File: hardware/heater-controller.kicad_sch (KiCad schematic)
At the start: 9 parts, among them J1 Vitotronic plug 96, Q1 SFH 309 FA

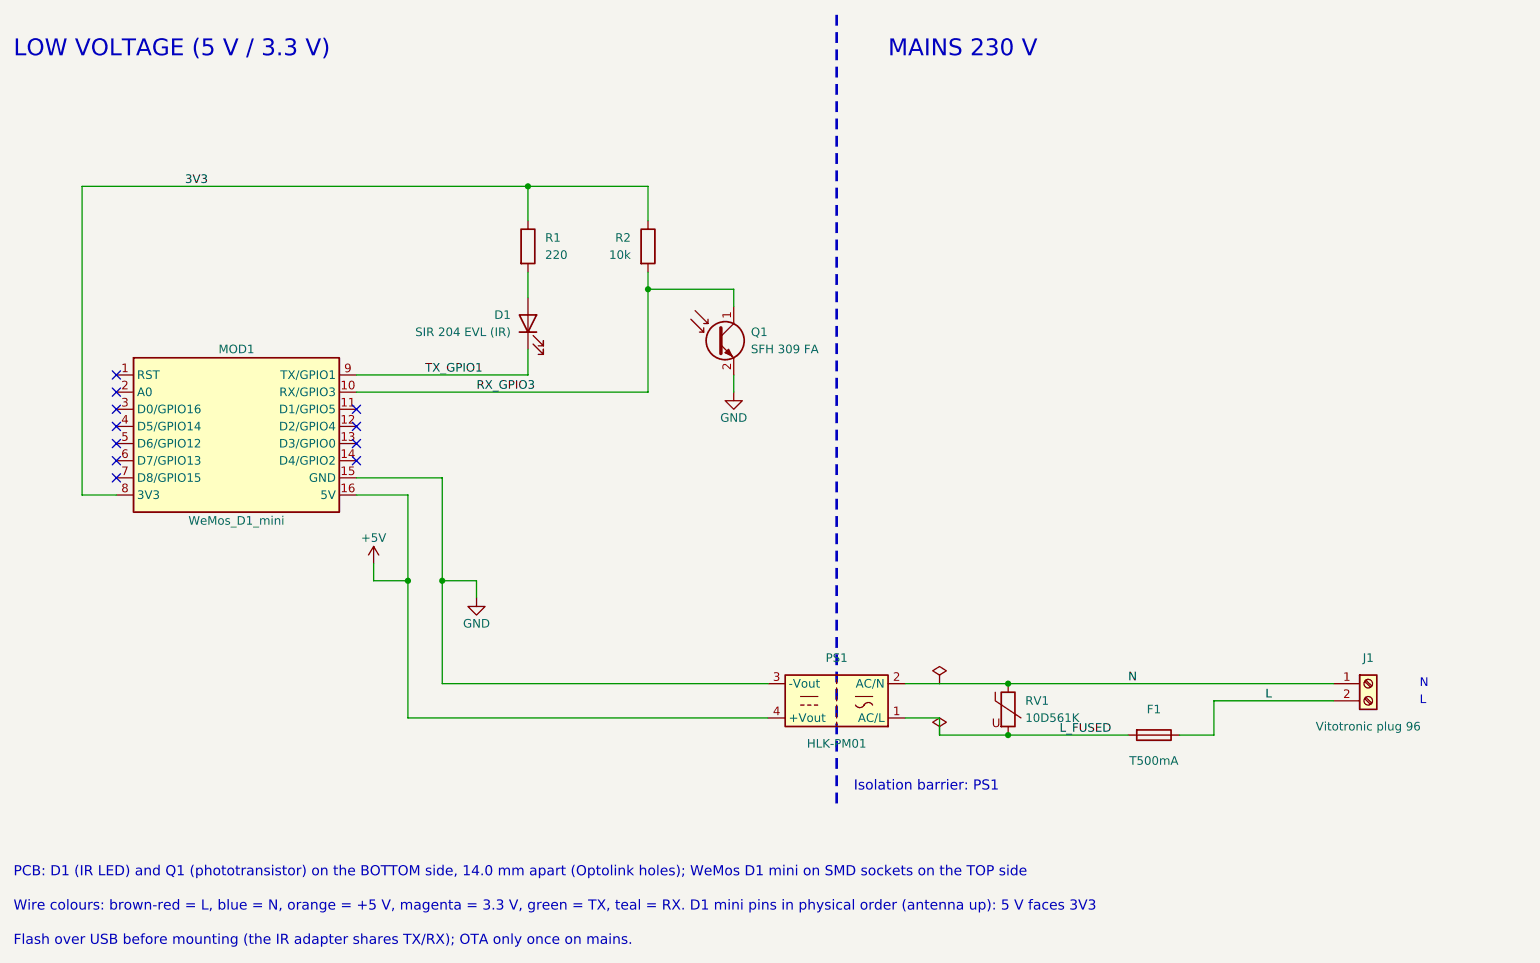
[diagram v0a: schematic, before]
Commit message: feat(hardware): move to ESP32-C3 on a removable U-shaped board
- ESP32-C3 super mini replaces the D1 mini: Optolink UART on GPIO4/GPIO3,
  logs over native USB
- inverted U board (86 x 39.5 mm): 230 V leg, optical head header on the bar,
  C3 on SMD female sockets; screw terminal for the mains wires
- off-board optical head on a 4-wire ribbon
- back GND pour, 0.7 mm power tracks, 6 mm mains isolation checked by DRC
- C3 socket footprint generator and fabrication export script
- enclosure redrawn around the new board
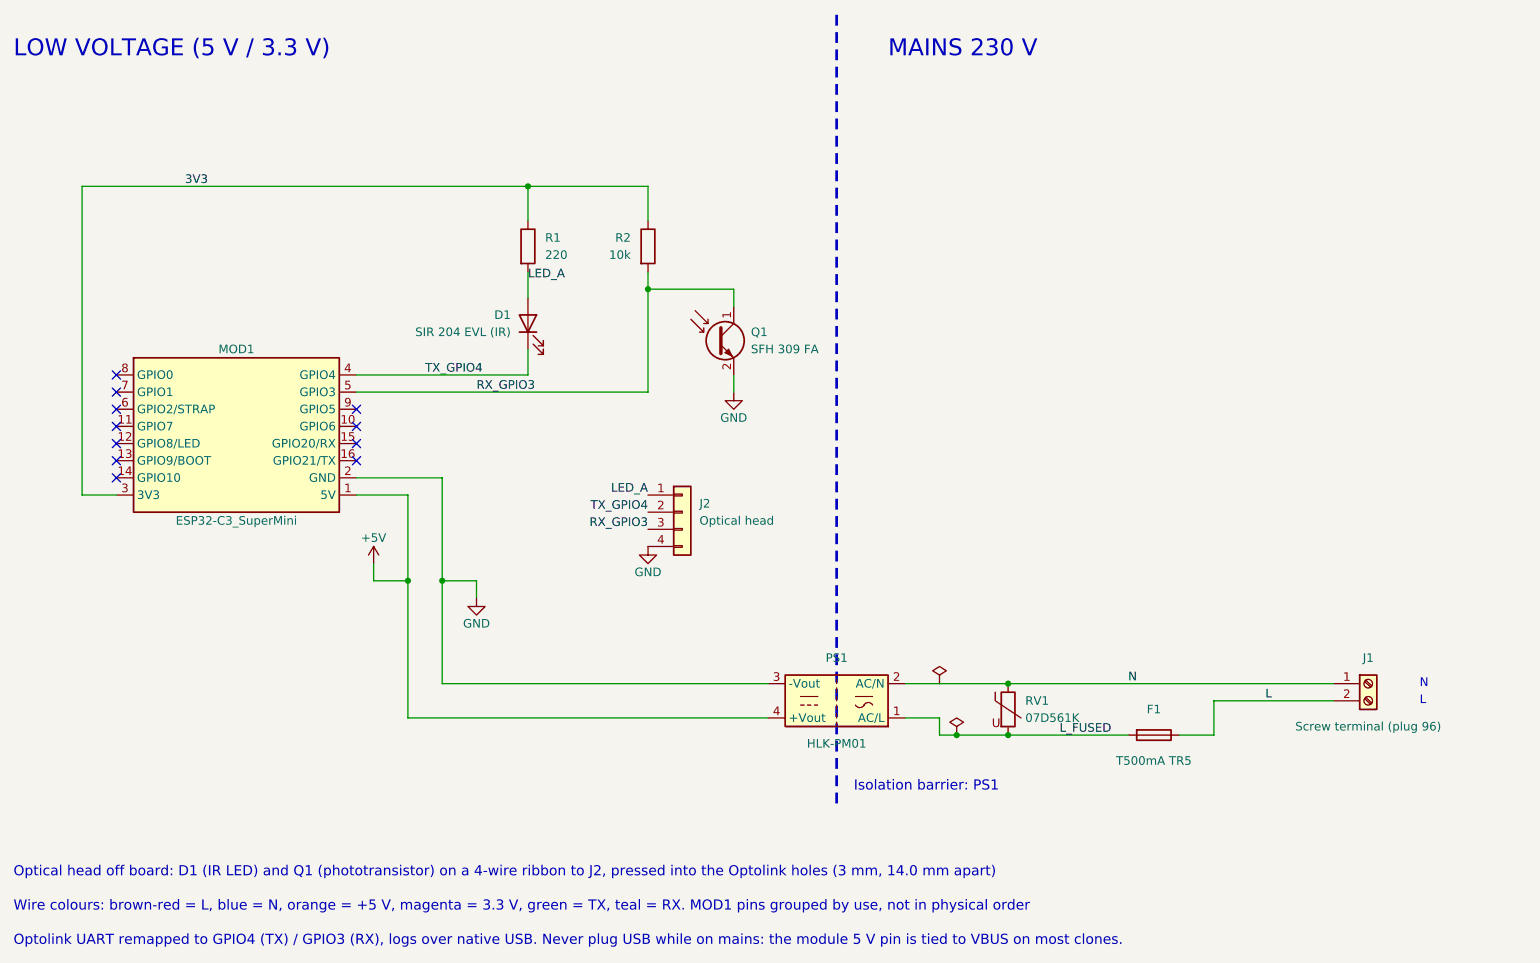
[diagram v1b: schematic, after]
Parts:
- added J2: Optical head, Connector_PinHeader_2.54mm:PinHeader_1x04_P2.54mm_Vertical, symbol Connector_Generic:Conn_01x04
- F1: value T500mA -> T500mA TR5; footprint Fuse:Fuseholder_Cylinder-5x20mm_Bulgin_FX0456_Vertical_Closed -> Fuse:Fuseholder_TR5_Littelfuse_No560_No460
- J1: value Vitotronic plug 96 -> Screw terminal (plug 96)
- MOD1: value WeMos_D1_mini -> ESP32-C3_SuperMini; footprint heater-controller:WEMOS_D1_mini_SMD_sockets -> heater-controller:ESP32-C3_SuperMini_Sockets; symbol heater-controller:WeMos_D1_mini -> heater-controller:ESP32-C3_SuperMini
- RV1: value 10D561K -> 07D561K; footprint Varistor:RV_Disc_D12mm_W4.2mm_P7.5mm -> Varistor:RV_Disc_D9mm_W4.1mm_P5mm
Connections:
- net +5V: now also MOD1.1 (5V); no longer MOD1.16 (5V)
- net 3V3: now also MOD1.3 (3V3); no longer MOD1.8 (3V3)
- net GND: now also MOD1.2 (GND), J2.4 (Pin_4); no longer MOD1.15 (GND)
- net RX_GPIO3: now also MOD1.5 (GPIO3), J2.3 (Pin_3); no longer MOD1.10 (RX/GPIO3)
- net TX_GPIO4: now reaches MOD1.4 (GPIO4)
- net TX_GPIO4: now also D1.1 (K), J2.2 (Pin_2)
- net LED_A: now reaches D1.2 (A), R1.2
- net LED_A: now also J2.1 (Pin_1)
- net TX_GPIO1: no longer names the net of MOD1.9 (GPIO5)
- net TX_GPIO1: no longer D1.1 (K)
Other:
- note added: "Optical head off board: D1 (IR LED) and Q1 (phototransistor) on a 4-wire ribbon to J2, pressed into the Optolink holes (3 mm, 14.0 mm apart)"
- note added: "Optolink UART remapped to GPIO4 (TX) / GPIO3 (RX), logs over native USB. Never plug USB while on mains: the module 5 V pin is tied to VBUS on most clones."
- note added: "Wire colours: brown-red = L, blue = N, orange = +5 V, magenta = 3.3 V, green = TX, teal = RX. MOD1 pins grouped by use, not in physical order"
- note removed: "Flash over USB before mounting (the IR adapter shares TX/RX); OTA only once on mains."
- note removed: "PCB: D1 (IR LED) and Q1 (phototransistor) on the BOTTOM side, 14.0 mm apart (Optolink holes); WeMos D1 mini on SMD sockets on the TOP side"
- note removed: "Wire colours: brown-red = L, blue = N, orange = +5 V, magenta = 3.3 V, green = TX, teal = RX. D1 mini pins in physical order (antenna up): 5 V faces 3V3"

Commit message: feat(hardware): hand-solderable board with SMD C3 sockets for JLCPCB
- C3 plugged into two hanxia 1x8 SMD sockets (J3/J4) at 15.24 mm, the only
  parts with an LCSC number; MOD1 off board with a board-only outline
- through-hole everything else: TR5 T1A fuse, 07D431K varistor, JST PH
  vertical optical head connector, axial resistors
- HLK-PM01 footprint from the Hi-Link datasheet (15.4 / 29.4 mm pin pitch)
- footprints generated by footprints.py from the datasheets
- export adds the JLCPCB BOM and placement files
- routing done in KiCad: 0.7 mm power tracks, no ground plane
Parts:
- added J3: Socket 1x8 SMD (C3 pins 1-8), heater-controller:PinSocket_1x08_P2.54mm_SMD_HX-ZQ, symbol Connector_Generic:Conn_01x08
- added J4: Socket 1x8 SMD (C3 pins 9-16), heater-controller:PinSocket_1x08_P2.54mm_SMD_HX-ZQ, symbol Connector_Generic:Conn_01x08
- D1, Q1: now left out of the parts list
- F1: value T500mA TR5 -> T1A TR5
- J2: value Optical head -> Optical head JST PH 4P; footprint Connector_PinHeader_2.54mm:PinHeader_1x04_P2.54mm_Vertical -> Connector_JST:JST_PH_B4B-PH-K_1x04_P2.00mm_Vertical
- MOD1: footprint heater-controller:ESP32-C3_SuperMini_Sockets -> (none); now left out of the parts list
- PS1: footprint Converter_ACDC:Converter_ACDC_Hi-Link_HLK-PMxx -> heater-controller:Converter_ACDC_HLK-PM01
- R1, R2: footprint Resistor_SMD:R_0805_2012Metric -> Resistor_THT:R_Axial_DIN0207_L6.3mm_D2.5mm_P7.62mm_Horizontal
- RV1: value 07D561K -> 07D431K (275VAC); footprint Varistor:RV_Disc_D9mm_W4.1mm_P5mm -> Varistor:RV_Disc_D7mm_W4.3mm_P5mm
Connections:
- net +5V: now also J3.1 (Pin_1)
- net 3V3: now also J3.3 (Pin_3)
- net GND: now also J3.2 (Pin_2)
- net RX_GPIO3: now also J3.5 (Pin_5)
- net TX_GPIO4: now also J3.4 (Pin_4)
- no-connect marks 11 -> 22

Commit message: feat(hardware): source every part at LCSC with datasheet footprints
- Kefa KF128 terminal block (Phoenix MKDS out of stock), Bourns MOV-07D431K
  inline varistor and JST PH with 0.9 mm holes, drawn by footprints.py
- LCSC number on every part; split-bom.py writes the JLCPCB BOM (SMD only)
  and an LCSC cart for the hand-soldered parts
- RV1 rerouted for its inline leads; DRC clean, schematic parity
- Enclosure split into named bodies: shells, lid, optical plug
- READMEs: parts list with suppliers, prices and footprint specs
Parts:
- F1: value T1A TR5 -> TR5 holder + T1A fuse; LCSC (none) -> C142909
- J1: value Screw terminal (plug 96) -> KF128-5.08 (plug 96); footprint TerminalBlock_Phoenix:TerminalBlock_Phoenix_MKDS-1,5-2-5.08_1x02_P5.08mm_Horizontal -> heater-controller:TerminalBlock_Kefa_KF128-5.08_1x02; LCSC (none) -> C474952
- J2: value Optical head JST PH 4P -> JST B4B-PH-K (optical head); footprint Connector_JST:JST_PH_B4B-PH-K_1x04_P2.00mm_Vertical -> heater-controller:JST_PH_B4B-PH-K_1x04_P2.00mm_Vertical_Drill0.9; LCSC (none) -> C131334
- PS1: LCSC (none) -> C209903
- RV1: value 07D431K (275VAC) -> MOV-07D431K (275VAC); footprint Varistor:RV_Disc_D7mm_W4.3mm_P5mm -> heater-controller:RV_Disc_D9mm_W4.8mm_P5mm_Inline; LCSC (none) -> C1528105
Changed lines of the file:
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@@
 			)
 		)
-		(property "Value" "Screw terminal (plug 96)"
+		(property "Value" "KF128-5.08 (plug 96)"
 			(at 231.14 130.81 0)
 			(show_name no)
@@
 			)
 		)
-		(property "Footprint" "TerminalBlock_Phoenix:TerminalBlock_Phoenix_MKDS-1,5-2-5.08_1x02_P5.08mm_Horizontal"
+		(property "Footprint" "heater-controller:TerminalBlock_Kefa_KF128-5.08_1x02"
 			(at 231.14 124.46 0)
 			(hide yes)
@@
 			)
 		)
+		(property "LCSC" "C474952"
+			(at 231.14 124.46 0)
+			(effects
+				(font
+					(size 1.27 1.27)
+				)
+				(hide yes)
+			)
+		)
 		(property "Description" ""
 			(at 231.14 124.46 0)
@@
 			)
 		)
-		(property "Value" "07D431K (275VAC)"
+		(property "Value" "MOV-07D431K (275VAC)"
 			(at 180.34 129.54 0)
 			(show_name no)
@@
 			)
 		)
-		(property "Footprint" "Varistor:RV_Disc_D7mm_W4.3mm_P5mm"
+		(property "Footprint" "heater-controller:RV_Disc_D9mm_W4.8mm_P5mm_Inline"
 			(at 177.8 128.27 0)
 			(hide yes)
@@
 			)
 		)
+		(property "LCSC" "C1528105"
+			(at 177.8 128.27 0)
+			(effects
+				(font
+					(size 1.27 1.27)
+				)
+				(hide yes)
+			)
+		)
 		(property "Description" ""
 			(at 177.8 128.27 0)
@@
 			)
 		)
+		(property "LCSC" "C209903"
+			(at 152.4 127 0)
+			(effects
+				(font
+					(size 1.27 1.27)
+				)
+				(hide yes)
+			)
+		)
 		(property "Description" ""
 			(at 152.4 127 0)
@@
 			)
 		)
-		(property "Value" "T1A TR5"
+		(property "Value" "TR5 holder + T1A fuse"
 			(at 199.39 135.89 90)
 			(show_name no)
@@
 			)
 		)
+		(property "LCSC" "C142909"
+			(at 199.39 132.08 0)
+			(effects
+				(font
+					(size 1.27 1.27)
+				)
+				(hide yes)
+			)
+		)
 		(property "Description" ""
 			(at 199.39 132.08 0)
@@
 			)
 		)
-		(property "Value" "Optical head JST PH 4P"
+		(property "Value" "JST B4B-PH-K (optical head)"
 			(at 132.08 100.33 0)
 			(show_name no)
@@
 			)
 		)
-		(property "Footprint" "Connector_JST:JST_PH_B4B-PH-K_1x04_P2.00mm_Vertical"
+		(property "Footprint" "heater-controller:JST_PH_B4B-PH-K_1x04_P2.00mm_Vertical_Drill0.9"
 			(at 129.54 99.06 0)
 			(hide yes)
@@
 			)
 		)
+		(property "LCSC" "C131334"
+			(at 129.54 99.06 0)
+			(effects
+				(font
+					(size 1.27 1.27)
+				)
+				(hide yes)
+			)
+		)
